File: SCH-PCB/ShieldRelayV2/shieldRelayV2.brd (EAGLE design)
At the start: 99.1 x 84.1 mm, 89 parts, among them IC1 LM2596SX-5.0_NOPB, IC2 LM1117MPX-33NOPB, IC3 FT231XS-R, K1 SLA-05VDC-SL-C, K2 SRD-05VDC-SL-C, K3 G3MB-202PL-DC5, K5 G3MB-202PL-DC5, K6 SRD-05VDC-SL-C, Q1 MMST2222A-7-F, Q2 MMST2222A-7-F, Q3 MMST2222A-7-F, Q4 MMST2222A-7-F, Q5 MMST2222A-7-F, Q6 MMBT3904-TP, Q7 MMBT3904-TP

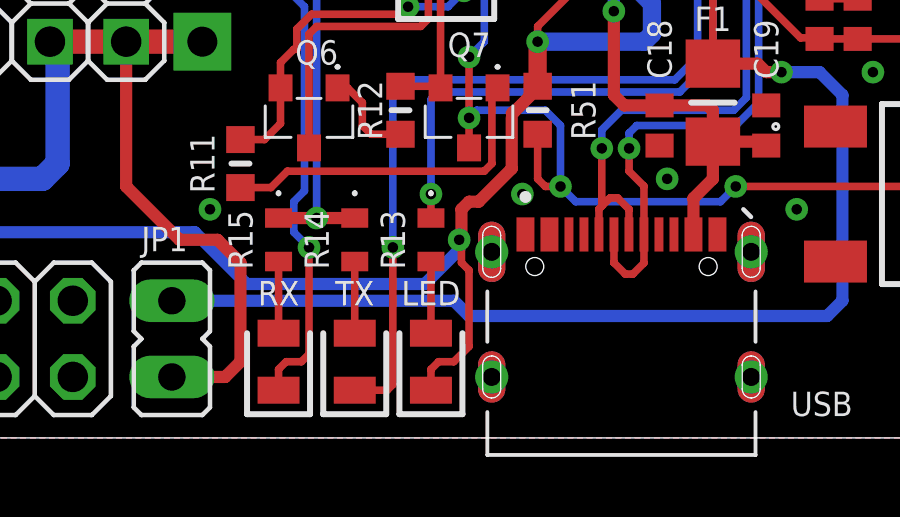
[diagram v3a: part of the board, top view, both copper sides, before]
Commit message: FIX: fix led pin io2 ond katoda connected to 3v3 otherwise gns
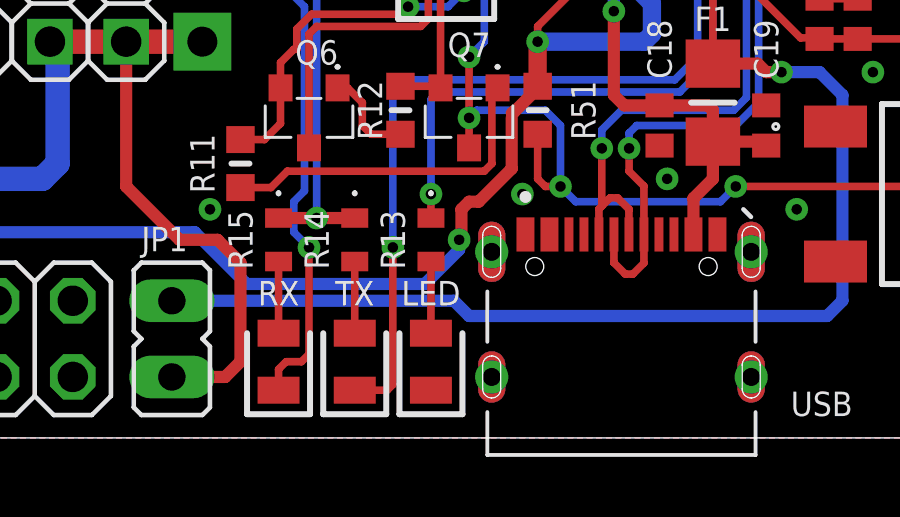
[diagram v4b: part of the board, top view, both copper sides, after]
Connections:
- net +3V3: no longer LED.1
- net GND: now also LED.1, USB.S1, USB.S2, USB.S3, USB.S4
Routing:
- net +3V3: track 145.8 -> 139.9 mm
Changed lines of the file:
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@@
 <drawing>
 <settings>
-<setting alwaysvectorfont="no"/>
+<setting alwaysvectorfont="yes"/>
 <setting verticaltext="up"/>
 </settings>
@@
 </layers>
 <board>
-<fusionsync huburn="a.YnVzaW5lc3M6Z21haWwyMzM3NTk" projecturn="a.YnVzaW5lc3M6Z21haWwyMzM3NTkjRDIwMTkwNzEwMjAyOTg4NzI2" f3durn="urn:adsk.wipprod:dm.lineage:9T0BP-n2RnCNxMkO3_9ujQ" pcbguid="" lastpulledtime="" lastsyncedchangeguid="" latestrevisionid="43e5cbbb-d091-4418-b876-1ea316f0a193" lastsyncedrevisionid="43e5cbbb-d091-4418-b876-1ea316f0a193" lastboardhashguid="19c69a16-bb44-e2b6-368f-cff3622da438" lastpushedtime="2024-06-15T15:23:29Z" linktopcb3d="false"/>
+<fusionsync huburn="a.YnVzaW5lc3M6Z21haWwyMzM3NTk" projecturn="a.YnVzaW5lc3M6Z21haWwyMzM3NTkjRDIwMTkwNzEwMjAyOTg4NzI2" f3durn="urn:adsk.wipprod:dm.lineage:9T0BP-n2RnCNxMkO3_9ujQ" pcbguid="" lastpulledtime="" lastsyncedchangeguid="" latestrevisionid="43e5cbbb-d091-4418-b876-1ea316f0a193" lastsyncedrevisionid="43e5cbbb-d091-4418-b876-1ea316f0a193" lastboardhashguid="19c69a16-bb44-e2b6-368f-cff3622da438" lastpushedtime="2024-06-15T15:23:29Z" linktopcb3d="true"/>
 <plain>
 <wire x1="78.74" y1="23.368" x2="78.486" y2="23.622" width="0.1524" layer="21"/>
@@
 <via x="34.544" y="59.436" extent="1-16" drill="0.35"/>
 <contactref element="IC2" pad="1"/>
+<contactref element="LED" pad="1"/>
+<contactref element="USB" pad="S1"/>
+<contactref element="USB" pad="S4"/>
+<contactref element="USB" pad="S2"/>
+<contactref element="USB" pad="S3"/>
 </signal>
 <signal name="N$2">
@@
 <contactref element="C4" pad="2"/>
 <wire x1="81.026" y1="29.302" x2="82.296" y2="29.302" width="0.254" layer="1"/>
-<contactref element="LED" pad="1"/>
 <contactref element="R51" pad="1"/>
 <contactref element="ESP32" pad="2"/>
@@
 <wire x1="78.994" y1="34.29" x2="78.994" y2="30.734" width="0.254" layer="1"/>
 <wire x1="78.994" y1="30.734" x2="80.391" y2="29.337" width="0.254" layer="1"/>
-<wire x1="68.072" y1="17.592" x2="68.072" y2="18.288" width="0.254" layer="1"/>
-<wire x1="68.072" y1="18.288" x2="68.326" y2="18.542" width="0.254" layer="1"/>
-<wire x1="68.834" y1="18.542" x2="69.342" y2="19.05" width="0.254" layer="1"/>
-<wire x1="69.342" y1="21.59" x2="69.088" y2="21.844" width="0.254" layer="1"/>
-<wire x1="69.088" y1="21.844" x2="69.088" y2="22.606" width="0.254" layer="1"/>
-<wire x1="68.326" y1="18.542" x2="68.834" y2="18.542" width="0.254" layer="1"/>
-<wire x1="69.342" y1="19.05" x2="69.342" y2="21.59" width="0.254" layer="1"/>
 <wire x1="70.7644" y1="26.8224" x2="70.7644" y2="26.67" width="0.254" layer="1"/>
 <wire x1="69.088" y1="22.606" x2="69.0124" y2="22.606" width="0.254" layer="1"/>

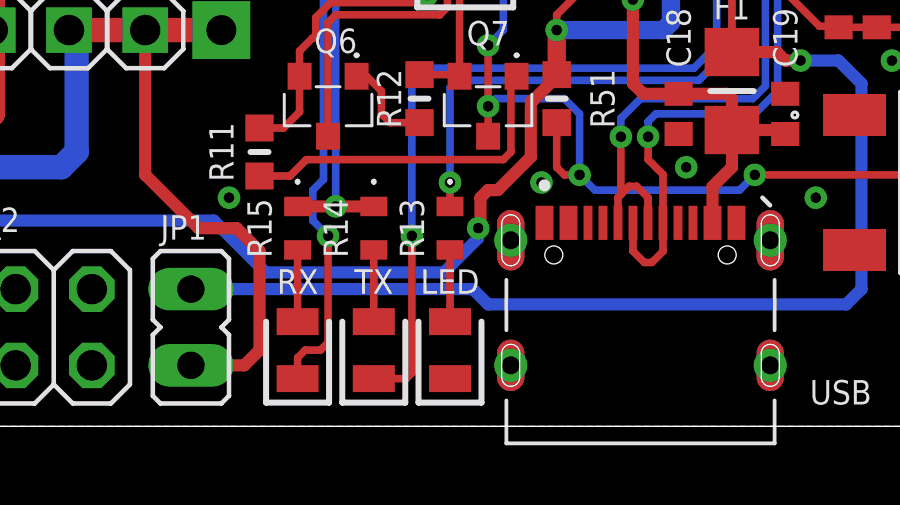
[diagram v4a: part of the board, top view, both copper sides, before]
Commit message: FIX: fix led pin io2 ond katoda connected to 3v3 otherwise gns
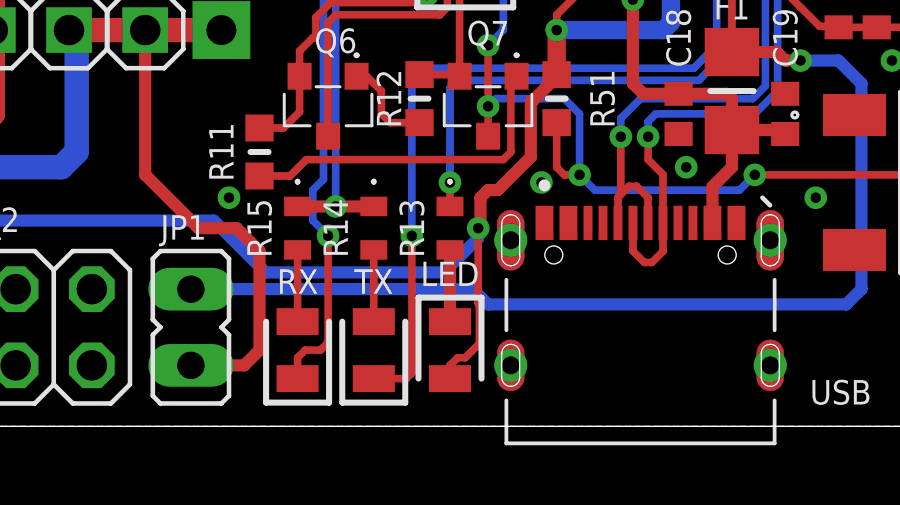
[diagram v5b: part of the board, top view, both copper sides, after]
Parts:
- turned LED to 270 degrees
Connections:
- removed net N$34: LED.2, R13.2
- new net N$22: LED.1, R13.2
- net +3V3: now also LED.2
- net GND: no longer LED.1
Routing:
- net +3V3: track 139.9 -> 145.5 mm
- net N$34: track 2.39 -> 0.00 mm
- net N$22: track 0.00 -> 2.39 mm
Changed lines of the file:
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@@
 <drawing>
 <settings>
-<setting alwaysvectorfont="yes"/>
+<setting alwaysvectorfont="no"/>
 <setting verticaltext="up"/>
 </settings>
@@
 </layers>
 <board>
-<fusionsync huburn="a.YnVzaW5lc3M6Z21haWwyMzM3NTk" projecturn="a.YnVzaW5lc3M6Z21haWwyMzM3NTkjRDIwMTkwNzEwMjAyOTg4NzI2" f3durn="urn:adsk.wipprod:dm.lineage:9T0BP-n2RnCNxMkO3_9ujQ" pcbguid="" lastpulledtime="" lastsyncedchangeguid="" latestrevisionid="43e5cbbb-d091-4418-b876-1ea316f0a193" lastsyncedrevisionid="43e5cbbb-d091-4418-b876-1ea316f0a193" lastboardhashguid="19c69a16-bb44-e2b6-368f-cff3622da438" lastpushedtime="2024-06-15T15:23:29Z" linktopcb3d="true"/>
+<fusionsync huburn="a.YnVzaW5lc3M6Z21haWwyMzM3NTk" projecturn="a.YnVzaW5lc3M6Z21haWwyMzM3NTkjRDIwMTkwNzEwMjAyOTg4NzI2" f3durn="urn:adsk.wipprod:dm.lineage:9T0BP-n2RnCNxMkO3_9ujQ" pcbguid="" lastpulledtime="" lastsyncedchangeguid="" latestrevisionid="43e5cbbb-d091-4418-b876-1ea316f0a193" lastsyncedrevisionid="43e5cbbb-d091-4418-b876-1ea316f0a193" lastboardhashguid="19c69a16-bb44-e2b6-368f-cff3622da438" lastpushedtime="2024-06-15T15:23:29Z" linktopcb3d="false"/>
 <plain>
 <wire x1="78.74" y1="23.368" x2="78.486" y2="23.622" width="0.1524" layer="21"/>
@@
 <attribute name="VALUE" x="68.072" y="22.606" size="1.27" layer="27" rot="R270" align="center"/>
 </element>
-<element name="LED" library="AccesControlNFC" library_urn="urn:adsk.eagle:library:37185839" package="LEDC2012X80N" package3d_urn="urn:adsk.eagle:package:22724977/2" value="Green" x="68.072" y="18.542" smashed="yes" rot="R90">
-<attribute name="DESCRIPTION" value="LED,Wurth Elektronik,150080BS75000 Wurth Elektronik 150080BS75000, WL-SMCW Series Blue LED, 470 nm 2012 (0805) Clear, Rectangle Lens SMD package" x="24.13" y="-43.688" size="1.778" layer="27" rot="R90" display="off"/>
-<attribute name="HEIGHT" value="0.8mm" x="24.13" y="-43.688" size="1.778" layer="27" rot="R90" display="off"/>
-<attribute name="MANUFACTURER_NAME" value="Wurth Elektronik" x="24.13" y="-43.688" size="1.778" layer="27" rot="R90" display="off"/>
-<attribute name="MANUFACTURER_PART_NUMBER" value="150080BS75000" x="24.13" y="-43.688" size="1.778" layer="27" rot="R90" display="off"/>
-<attribute name="MOUSER_PART_NUMBER" value="710-150080BS75000" x="24.13" y="-43.688" size="1.778" layer="27" rot="R90" display="off"/>
-<attribute name="MOUSER_PRICE-STOCK" value="https://www.mouser.co.uk/ProductDetail/Wurth-Elektronik/150080BS75000?qs=2kOmHSv6VfT2tBo3UPVqAQ%3D%3D" x="24.13" y="-43.688" size="1.778" layer="27" rot="R90" display="off"/>
-<attribute name="NAME" x="68.072" y="20.828" size="0.8128" layer="25" rot="R180" align="center"/>
-<attribute name="VALUE" x="68.072" y="18.542" size="1.27" layer="27" rot="R90" align="center"/>
+<element name="LED" library="AccesControlNFC" library_urn="urn:adsk.eagle:library:37185839" package="LEDC2012X80N" package3d_urn="urn:adsk.eagle:package:22724977/2" value="Green" x="68.072" y="18.542" smashed="yes" rot="R270">
+<attribute name="DESCRIPTION" value="LED,Wurth Elektronik,150080BS75000 Wurth Elektronik 150080BS75000, WL-SMCW Series Blue LED, 470 nm 2012 (0805) Clear, Rectangle Lens SMD package" x="112.014" y="80.772" size="1.778" layer="27" rot="R270" display="off"/>
+<attribute name="HEIGHT" value="0.8mm" x="112.014" y="80.772" size="1.778" layer="27" rot="R270" display="off"/>
+<attribute name="MANUFACTURER_NAME" value="Wurth Elektronik" x="112.014" y="80.772" size="1.778" layer="27" rot="R270" display="off"/>
+<attribute name="MANUFACTURER_PART_NUMBER" value="150080BS75000" x="112.014" y="80.772" size="1.778" layer="27" rot="R270" display="off"/>
+<attribute name="MOUSER_PART_NUMBER" value="710-150080BS75000" x="112.014" y="80.772" size="1.778" layer="27" rot="R270" display="off"/>
+<attribute name="MOUSER_PRICE-STOCK" value="https://www.mouser.co.uk/ProductDetail/Wurth-Elektronik/150080BS75000?qs=2kOmHSv6VfT2tBo3UPVqAQ%3D%3D" x="112.014" y="80.772" size="1.778" layer="27" rot="R270" display="off"/>
+<attribute name="NAME" x="68.072" y="21.082" size="0.8128" layer="25" align="center"/>
+<attribute name="VALUE" x="68.072" y="18.542" size="1.27" layer="27" rot="R270" align="center"/>
 </element>
 <element name="Q6" library="AccesControlNFC" library_urn="urn:adsk.eagle:library:37185839" package="SI2305TP" package3d_urn="urn:adsk.eagle:package:33010713/2" value="MMBT3904-TP" x="64.008" y="26.67" smashed="yes" rot="R180">
@@
 <via x="34.544" y="59.436" extent="1-16" drill="0.35"/>
 <contactref element="IC2" pad="1"/>
-<contactref element="LED" pad="1"/>
 <contactref element="USB" pad="S1"/>
 <contactref element="USB" pad="S4"/>
@@
 <wire x1="39.624" y1="30.988" x2="40.386" y2="31.75" width="0.4064" layer="1"/>
 <wire x1="39.624" y1="29.464" x2="39.624" y2="30.988" width="0.4064" layer="1"/>
+<contactref element="LED" pad="2"/>
+<wire x1="69.0124" y1="22.606" x2="69.0124" y2="20.09673125" width="0.254" layer="1"/>
+<wire x1="69.0124" y1="20.09673125" x2="69.0514" y2="20.05773125" width="0.254" layer="1"/>
+<wire x1="69.0514" y1="20.05773125" x2="69.0514" y2="18.7594" width="0.254" layer="1"/>
+<wire x1="68.58" y1="18.288" x2="68.326" y2="18.288" width="0.254" layer="1"/>
+<wire x1="68.326" y1="18.288" x2="68.072" y2="18.034" width="0.254" layer="1"/>
+<wire x1="68.072" y1="18.034" x2="68.072" y2="17.592" width="0.254" layer="1"/>
+<wire x1="69.0514" y1="18.7594" x2="68.58" y2="18.288" width="0.254" layer="1"/>
 </signal>
 <signal name="N$39">
@@
 <wire x1="65.532" y1="21.881" x2="65.532" y2="19.492" width="0.254" layer="1"/>
 </signal>
-<signal name="N$34">
-<contactref element="LED" pad="2"/>
-<contactref element="R13" pad="2"/>
-<wire x1="68.072" y1="21.881" x2="68.072" y2="19.492" width="0.254" layer="1"/>
-</signal>
 <signal name="3V3_OUT">
 <contactref element="R14" pad="1"/>
@@
 <wire x1="64.008" y1="65.786" x2="64.008" y2="72.898" width="0.1524" layer="16"/>
 </signal>
+<signal name="N$22">
+<contactref element="LED" pad="1"/>
+<contactref element="R13" pad="2"/>
+<wire x1="68.072" y1="21.881" x2="68.072" y2="19.492" width="0.4064" layer="1"/>
+</signal>
 </signals>

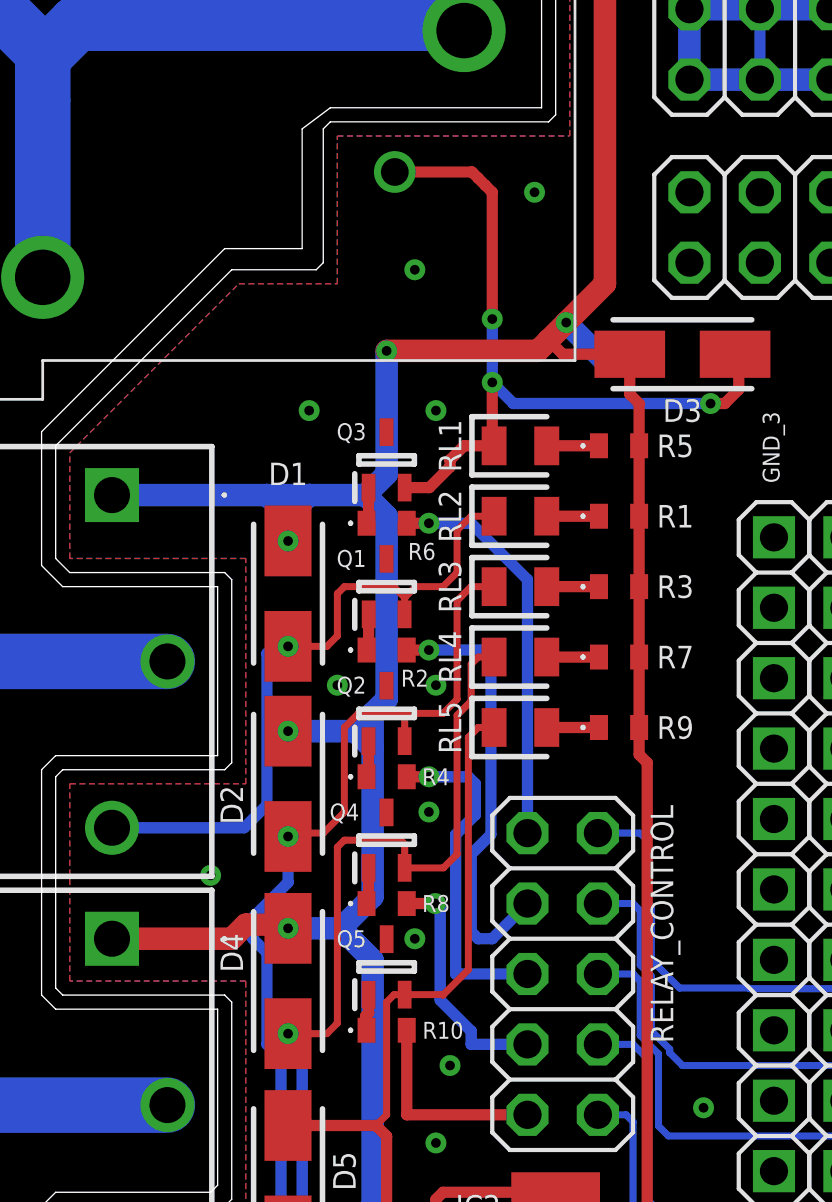
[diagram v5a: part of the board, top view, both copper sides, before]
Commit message: FIX: fix reverse transistor relay
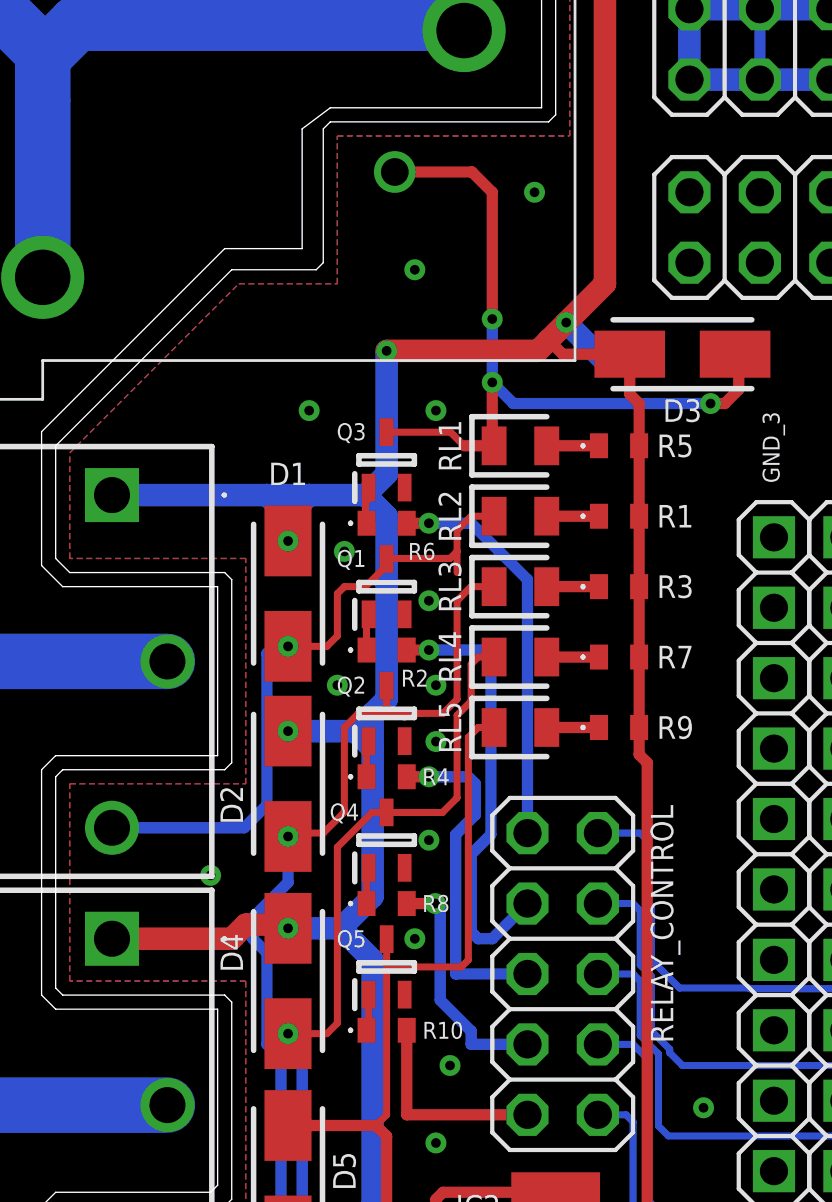
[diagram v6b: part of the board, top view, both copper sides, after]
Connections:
- net GND: now also Q1.2, Q2.2, Q3.2, Q4.2, Q5.2; no longer Q1.3, Q2.3, Q3.3, Q4.3, Q5.3
- net N$11: now also Q4.3; no longer Q4.2
- net N$14: now also Q5.3; no longer Q5.2
- net N$3: now also Q1.3; no longer Q1.2
- net N$5: now also Q2.3; no longer Q2.2
- net N$8: now also Q3.3; no longer Q3.2
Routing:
- net N$11: track 34.1 -> 31.6 mm
- net N$14: track 38.2 -> 39.7 mm
- net N$5: track 38.4 -> 39.3 mm
- net GND: vias 39 -> 42
